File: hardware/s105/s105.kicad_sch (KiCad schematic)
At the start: 0 parts

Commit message: наименование цепей разъема
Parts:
- added P? (x2): 368255-2, hellen121vag:368255-2, symbol 368255-2:368255-2
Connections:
- net +5V: now also P?.32, P?.33
- new net +12V: P?.63
- new net +12_Sens: P?.44
- new net AC_Press: P?.21
- new net AC_Relay: P?.69
- new net AFR_1: P?.18
- new net AFR_1_Heater: P?.48
- new net AFR_2: P?.55
- new net Absorber: P?.46
- new net Atart_dis_Relay: P?.50
- new net CAM_in: P?.79
- new net CAN_H: P?.62
- new net CAN_L: P?.81
- new net CEL: P?.31
- new net CLT: P?.39
- new net Crank_Sens+: P?.15
- new net Crank_Sens-: P?.34
- new net DCNS: P?.75
- new net DIN1: P?.72
- new net DIN5: P?.76
- new net DPH2: P?.73
- new net ECO/CLT_Out: P?.10
- new net Fan_Relay_1: P?.68
- new net Fan_relay_2/Unk_Out_2: P?.30
- new net Fuel_Pump_Relay: P?.70
- new net GND: P?.3, P?.61, P?.80
- new net GNDA: P?.17, P?.20, P?.35, P?.36, P?.51, P?.52, P?.53, P?.54
- new net IAT: P?.40
- new net IGN_1: P?.5
- new net IGN_2: P?.2
- new net IGN_3: P?.4
- new net IGN_4: P?.1
- new net IGN_swt: P?.13
- new net INJ_1: P?.27
- new net INJ_2: P?.6
- new net INJ_3: P?.7
- new net INJ_4: P?.47
- new net INJ_6/AFR_2_Heater: P?.49
- new net INJ_7: P?.25
- new net Idle_valve_close: P?.28
- new net Idle_valve_open: P?.29
- new net K-line: P?.71
- new net Knock: P?.19
- new net MAF: P?.37
- new net MAP: P?.56
- new net Prog_mode: P?.43
- new net Speed_in: P?.59
- new net Start_req: P?.77
- new net TACH: P?.8
- new net TPS: P?.16
- new net Unk_Out_1: P?.9
- no-connect marks 0 -> 51
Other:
- added sheet MCU (stm32.kicad_sch)

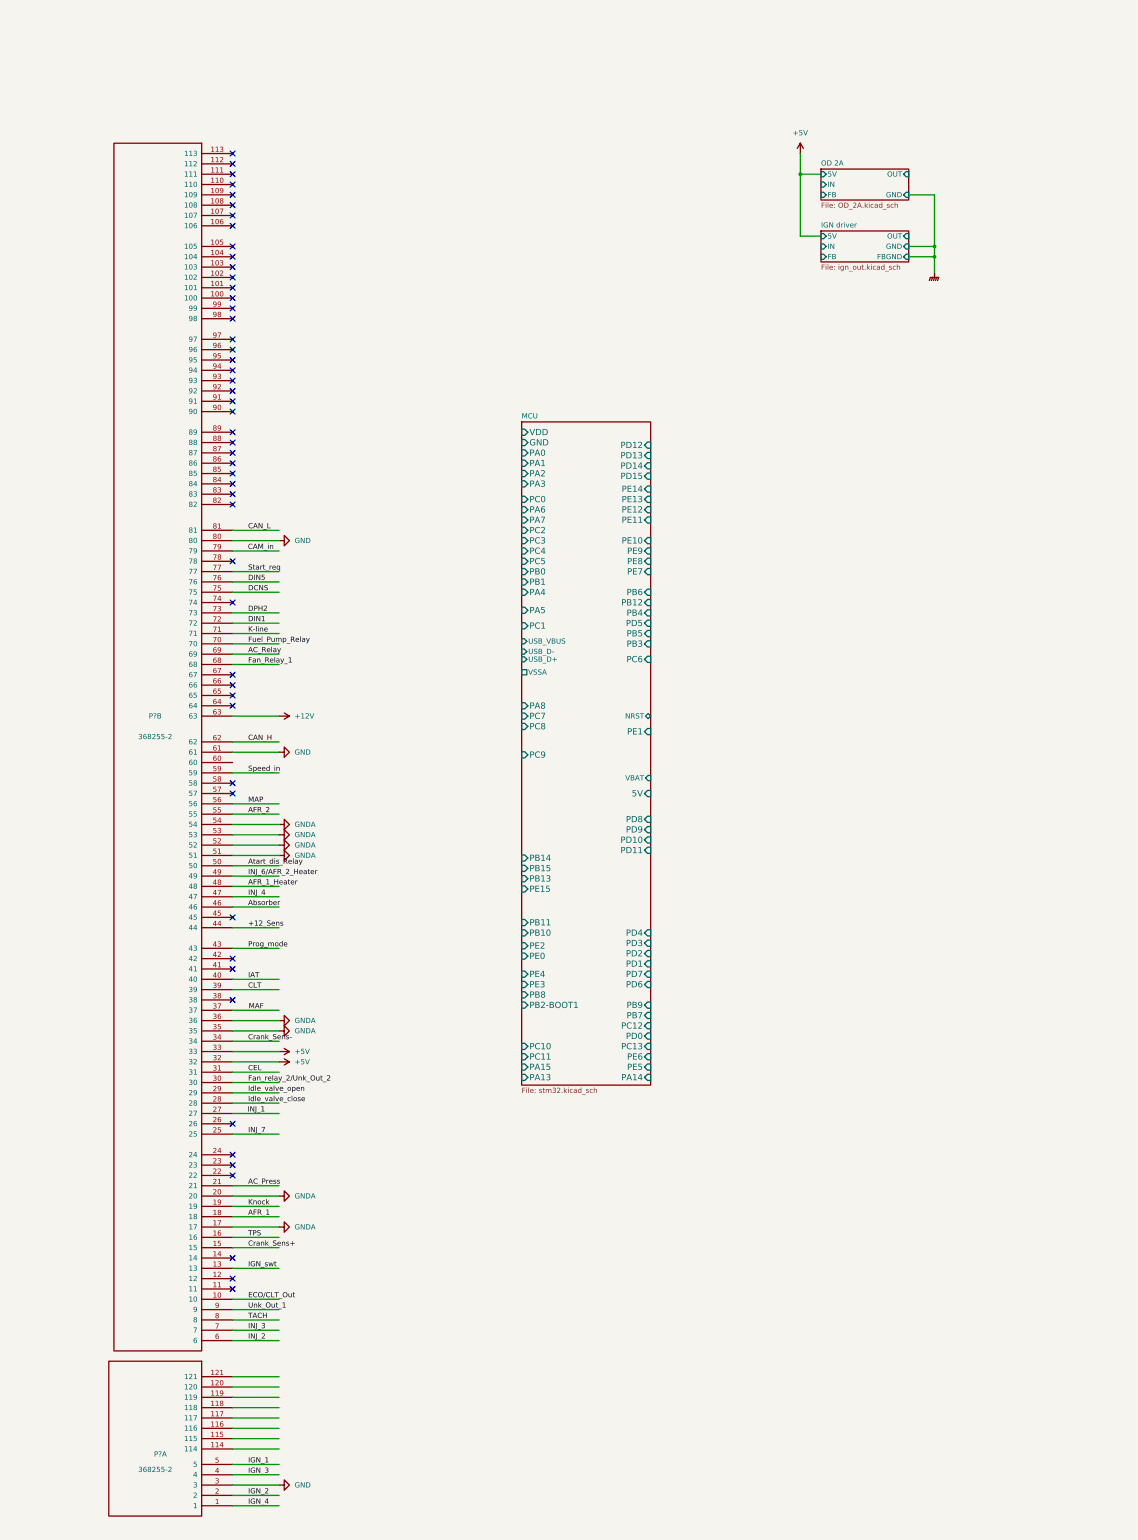
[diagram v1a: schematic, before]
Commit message: разместила схожие блоки
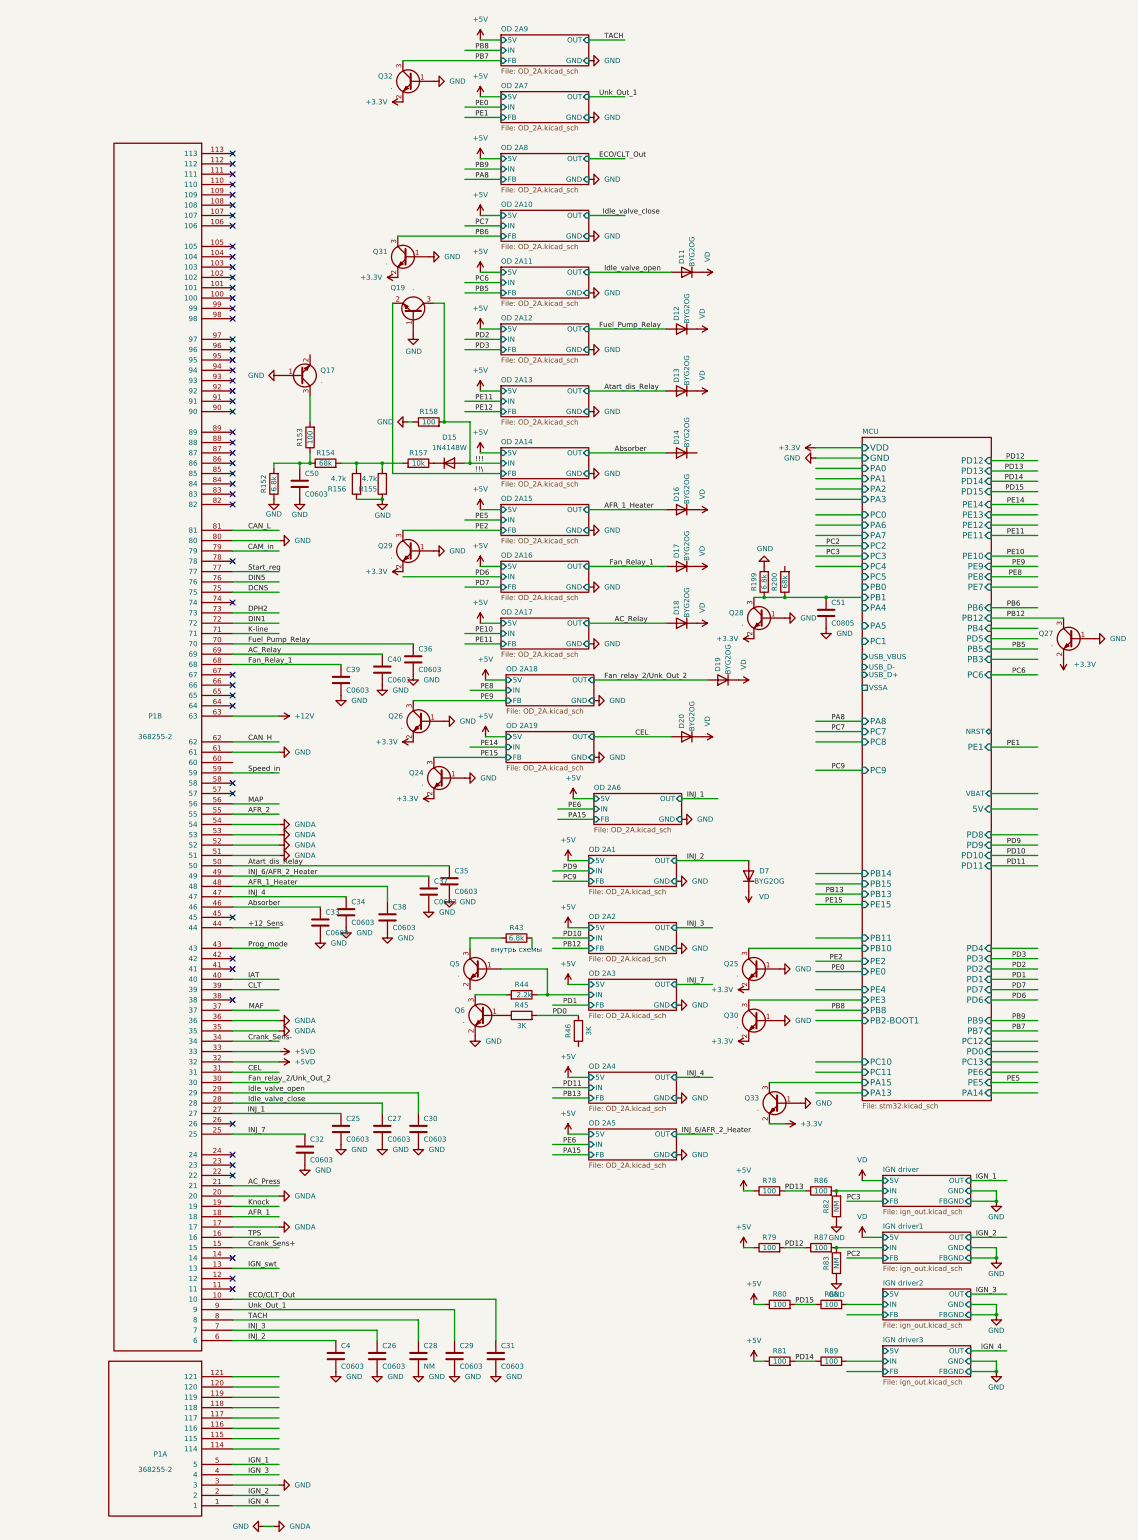
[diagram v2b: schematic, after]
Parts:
- added C25, C26, C27, C29, C30, C31, C32, C33, C34, C35, C36, C37, C38, C39, C4, C40, C50: C0603, Capacitor_SMD:C_0603_1608Metric, symbol Device:C
- added C28: NM, Capacitor_SMD:C_0603_1608Metric, symbol Device:C
- added C51: C0805, Capacitor_SMD:C_0805_2012Metric, symbol Device:C
- added D11, D12, D13, D14, D16, D17, D18, D19, D20, D7: BYG2OG, Diode_SMD:D_SMA, symbol Diode:US2JA
- added D15: 1N4148W, Diode_SMD:D_SOD-123, symbol Diode:1N4148W
- added Q17, Q19, Q24, Q25, Q26, Q27, Q28, Q29, Q30, Q31, Q32, Q33, Q5, Q6: ., Package_TO_SOT_SMD:SOT-23, symbol Transistor_BJT:BC847
- added R152, R199: 6.8k, Resistor_SMD:R_0603_1608Metric, symbol Device:R
- added R153, R158, R78, R79, R80, R81, R86, R87, R88, R89: 100, Resistor_SMD:R_0603_1608Metric, symbol Device:R
- added R154, R200: 68k, Resistor_SMD:R_0603_1608Metric, symbol Device:R
- added R155, R156: 4.7k, Resistor_SMD:R_1206_3216Metric, symbol Device:R
- added R157: 10k, Resistor_SMD:R_0805_2012Metric, symbol Device:R
- added R43: 6.8k, Resistor_SMD:R_0805_2012Metric, symbol Device:R
- added R44: 2.2k, Resistor_SMD:R_0805_2012Metric, symbol Device:R
- added R45, R46: 3K, Resistor_SMD:R_0603_1608Metric, symbol Device:R
- added R82, R83: NM, Resistor_SMD:R_0603_1608Metric, symbol Device:R
- gave numbers to parts that had none: 1
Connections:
- net GNDA is gone; now on net GND: P1.17, P1.20, P1.35, P1.36, P1.51, P1.52, P1.53, P1.54
- net +5V: now also R78.1, R79.1, R80.1, R81.1; no longer P1.32, P1.33
- net AC_Relay: now also C40.1, D18.2 (A)
- net AFR_1_Heater: now also C38.1, D16.2 (A)
- net Absorber: now also C33.1, D14.2 (A)
- net Atart_dis_Relay: now also C35.1, D13.2 (A)
- net CEL: now also D20.2 (A)
- net ECO/CLT_Out: now also C31.1
- net Fan_Relay_1: now also C39.1, D17.2 (A)
- net Fan_relay_2/Unk_Out_2: now also D19.2 (A)
- net Fuel_Pump_Relay: now also C36.1, D12.2 (A)
- net GND: now also C25.2, C26.2, C27.2, C28.2, C29.2, C30.2, C31.2, C32.2, C33.2, C34.2, C35.2, C36.2, C37.2, C38.2, C39.2, C4.2, C40.2, C50.2, C51.2, Q17.1 (B), Q19.1 (B), Q24.1 (B), Q25.1 (B), Q26.1 (B), Q27.1 (B), Q28.1 (B), Q29.1 (B), Q30.1 (B), Q31.1 (B), Q32.1 (B), Q33.1 (B), Q6.2 (E), R152.1, R155.1, R156.1, R158.1, R199.2, R82.1, R83.1
- net IGN driver/IN: now also R82.2, R86.2
- net INJ_1: now also C25.1
- net INJ_2: now also C4.1, D7.2 (A)
- net INJ_3: now also C26.1
- net INJ_4: now also C34.1
- net INJ_6/AFR_2_Heater: now also C37.1
- net INJ_7: now also C32.1
- net Idle_valve_close: now also C27.1
- net Idle_valve_open: now also C30.1, D11.2 (A)
- net MCU/PA15: now also Q33.3 (C)
- net MCU/PB1: now also C51.1, Q28.3 (C), R199.1, R200.1
- net MCU/PB10: now also Q25.3 (C)
- net MCU/PE3: now also Q30.3 (C)
- net TACH: now also C28.1
- net Unk_Out_1: now also C29.1
- new net: Q17.3 (C), R153.2
- new net: Q5.3 (C), R43.2
- new net: D15.1 (K), R157.1
- new net: R154.2, R155.2, R156.2, R157.2
- new net: C50.1, R152.2, R153.1, R154.1
- new net: Q6.1 (B), R45.1
- new net: Q6.3 (C), R44.2
- new net !!!: D15.2 (A), Q19.3 (C), R158.2
- new net !!\: Q19.2 (E)
- new net +3.3V: Q24.2 (E), Q25.2 (E), Q26.2 (E), Q27.2 (E), Q28.2 (E), Q29.2 (E), Q30.2 (E), Q31.2 (E), Q32.2 (E), Q33.2 (E)
- new net +5VD: P1.32, P1.33
- new net IGN driver1/IN: R83.2, R87.2
- new net IGN driver2/IN: R88.2
- new net IGN driver3/IN: R89.2
- new net OD 2A3/IN: Q5.1 (B), R44.1
- new net PB12: Q27.3 (C)
- new net PB6: Q31.3 (C)
- new net PB7: Q32.3 (C)
- new net PD0: R45.2, R46.2
- new net PD12: R79.2, R87.1
- new net PD13: R78.2, R86.1
- new net PD14: R81.2, R89.1
- new net PD15: R80.2, R88.1
- new net PE15: Q24.3 (C)
- new net PE2: Q29.3 (C)
- new net PE9: Q26.3 (C)
- new net VD: D11.1 (K), D12.1 (K), D13.1 (K), D16.1 (K), D17.1 (K), D18.1 (K), D19.1 (K), D20.1 (K), D7.1 (K)
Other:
- removed sheet OD 2A
- added sheet IGN driver1 (ign_out.kicad_sch)
- added sheet IGN driver2 (ign_out.kicad_sch)
- added sheet IGN driver3 (ign_out.kicad_sch)
- added sheet OD 2A1 (OD_2A.kicad_sch)
- added sheet OD 2A10 (OD_2A.kicad_sch)
- added sheet OD 2A11 (OD_2A.kicad_sch)
- added sheet OD 2A12 (OD_2A.kicad_sch)
- added sheet OD 2A13 (OD_2A.kicad_sch)
- added sheet OD 2A14 (OD_2A.kicad_sch)
- added sheet OD 2A15 (OD_2A.kicad_sch)
- added sheet OD 2A16 (OD_2A.kicad_sch)
- added sheet OD 2A17 (OD_2A.kicad_sch)
- added sheet OD 2A18 (OD_2A.kicad_sch)
- added sheet OD 2A19 (OD_2A.kicad_sch)
- added sheet OD 2A2 (OD_2A.kicad_sch)
- added sheet OD 2A3 (OD_2A.kicad_sch)
- added sheet OD 2A4 (OD_2A.kicad_sch)
- added sheet OD 2A5 (OD_2A.kicad_sch)
- added sheet OD 2A6 (OD_2A.kicad_sch)
- added sheet OD 2A7 (OD_2A.kicad_sch)
- added sheet OD 2A8 (OD_2A.kicad_sch)
- added sheet OD 2A9 (OD_2A.kicad_sch)
- note added: "внутрь схемы"

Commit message: вписала в габариты платы, продолжила опознание
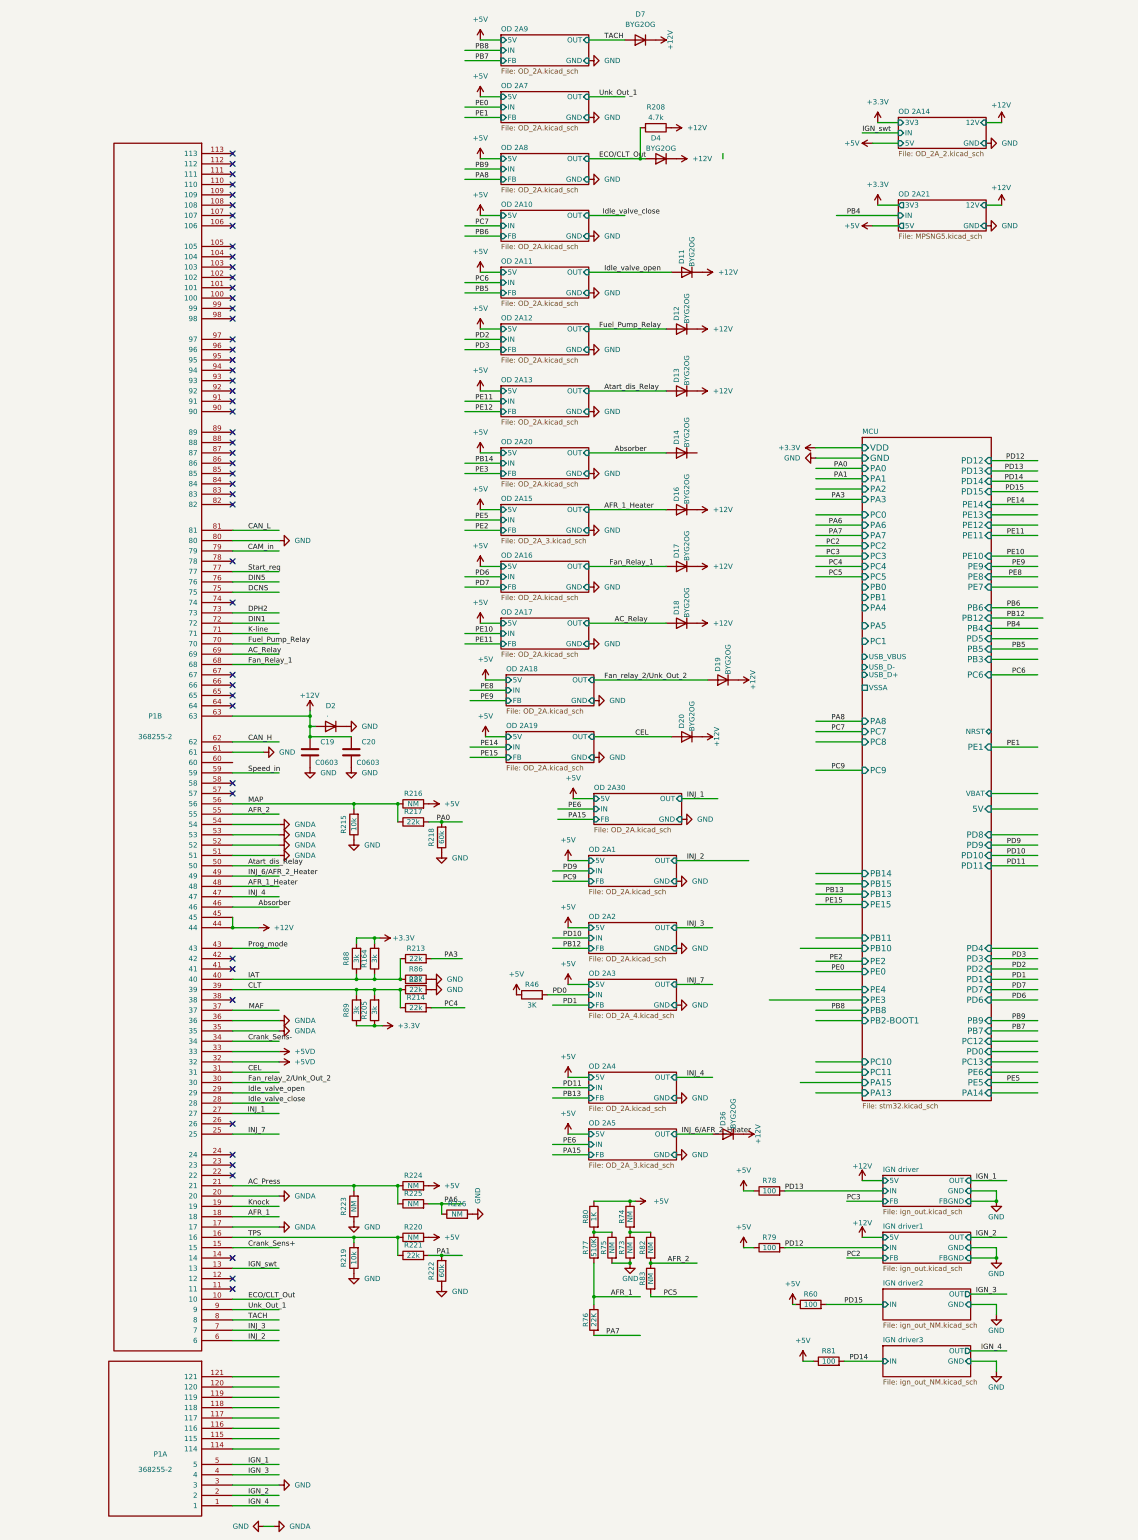
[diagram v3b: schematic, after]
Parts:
- removed C25, C26, C27, C29, C30, C31, C32, C33, C34, C35, C36, C37, C38, C39, C4, C40, C50: C0603, Capacitor_SMD:C_0603_1608Metric, symbol Device:C
- removed C28: NM, Capacitor_SMD:C_0603_1608Metric, symbol Device:C
- removed C51: C0805, Capacitor_SMD:C_0805_2012Metric, symbol Device:C
- removed D15: 1N4148W, Diode_SMD:D_SOD-123, symbol Diode:1N4148W
- removed Q17, Q19, Q24, Q25, Q26, Q27, Q28, Q29, Q30, Q31, Q32, Q33, Q5, Q6: ., Package_TO_SOT_SMD:SOT-23, symbol Transistor_BJT:BC847
- removed R152, R199: 6.8k, Resistor_SMD:R_0603_1608Metric, symbol Device:R
- removed R153, R158: 100, Resistor_SMD:R_0603_1608Metric, symbol Device:R
- removed R154, R200: 68k, Resistor_SMD:R_0603_1608Metric, symbol Device:R
- removed R155, R156: 4.7k, Resistor_SMD:R_1206_3216Metric, symbol Device:R
- removed R157: 10k, Resistor_SMD:R_0805_2012Metric, symbol Device:R
- removed R43: 6.8k, Resistor_SMD:R_0805_2012Metric, symbol Device:R
- removed R44: 2.2k, Resistor_SMD:R_0805_2012Metric, symbol Device:R
- removed R45: 3K, Resistor_SMD:R_0603_1608Metric, symbol Device:R
- added C19, C20: C0603, Capacitor_SMD:C_0603_1608Metric, symbol Device:C
- added D2: ., Diode_SMD:D_SMC, symbol Diode:US2JA
- added D36, D4: BYG2OG, Diode_SMD:D_SMA, symbol Diode:US2JA
- added R164, R205: 3k, Resistor_SMD:R_1206_3216Metric, symbol Device:R
- added R208: 4.7k, Resistor_SMD:R_1206_3216Metric, symbol Device:R
- added R213, R214, R217, R221: 22k, Resistor_SMD:R_0603_1608Metric, symbol Device:R
- added R215, R219: 10k, Resistor_SMD:R_0603_1608Metric, symbol Device:R
- added R216, R220, R223, R224, R225, R226, R73, R74, R75: NM, Resistor_SMD:R_0603_1608Metric, symbol Device:R
- added R218, R222: 60k, Resistor_SMD:R_0603_1608Metric, symbol Device:R
- added R60: 100, Resistor_SMD:R_0603_1608Metric, symbol Device:R
- added R76: 22K, Resistor_SMD:R_0603_1608Metric, symbol Device:R
- added R77: 510K, Resistor_SMD:R_0603_1608Metric, symbol Device:R
- R80: value 100 -> 1K; LCSC (none) -> C25804; Manufacturer (none) -> StackPole; Part # (none) -> RMCF0603JT10K0; VEND (none) -> DIGI; VEND# (none) -> RMCF0603JT10K0CT-ND
- R82, R83: LCSC (none) -> C25804; Manufacturer (none) -> StackPole; Part # (none) -> RMCF0603JT10K0; VEND (none) -> DIGI; VEND# (none) -> RMCF0603JT10K0CT-ND
- R86, R87: value 100 -> 22k
- R88, R89: value 100 -> 3k; footprint Resistor_SMD:R_0603_1608Metric -> Resistor_SMD:R_1206_3216Metric
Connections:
- net +12_Sens is gone; now on net +12V: P1.44
- net IGN driver2/IN is gone; now on net +3.3V: R88.2
- net IGN driver3/IN is gone; now on net CLT: R89.2
- net VD is gone; now on net +12V: D11.1 (K), D12.1 (K), D13.1 (K), D16.1 (K), D17.1 (K), D18.1 (K), D19.1 (K), D20.1 (K), D7.1 (K)
- net +12V: now also P1.45, C19.1, C20.1, D2.2 (A), D36.1 (K), D4.1 (K), R208.1
- net +3.3V: now also R89.1, R164.2, R205.1
- net +5V: now also R46.1, R216.2, R220.2, R224.2, R60.1, R74.1
- net AC_Press: now also R223.2, R224.1, R225.1
- net AFR_1: now also R76.1, R77.2
- net AFR_2: now also R82.2, R83.1
- net CLT: now also R87.1, R205.2, R214.1
- net ECO/CLT_Out: now also D4.2 (A), R208.2
- net GND: now also R86.2, R87.2, C19.2, C20.2, D2.1 (K), R215.1, R218.1, R219.1, R222.1, R223.1, R226.2, R73.2, R75.2; no longer R82.1, R83.1
- net IAT: now also R86.1, R88.1, R164.1, R213.1
- net INJ_2: no longer D7.2 (A)
- net INJ_6/AFR_2_Heater: now also D36.2 (A)
- net MAP: now also R215.2, R216.1, R217.1
- net PD12: no longer R87.1
- net PD13: no longer R86.1
- net PD14: no longer R89.1
- net PD15: now also R60.2; no longer R80.2, R88.1
- net TACH: now also D7.2 (A)
- net TPS: now also R219.2, R220.1, R221.1
- removed net IGN driver/IN: R82.2, R86.2
- net IGN driver1/IN renamed PC5
- net PC5: no longer R87.2
- new net: R73.1, R74.2, R82.1
- new net: R75.1, R77.1, R80.2
- new net PA0: R217.2, R218.2
- new net PA1: R221.2, R222.2
- new net PA3: R213.2
- new net PA6: R225.2, R226.1
- new net PA7: R76.2
- new net PC4: R214.2
- no-connect marks 51 -> 50
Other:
- sheet OD 2A6 renamed OD 2A30
- added sheet OD 2A20 (OD_2A.kicad_sch)
- added sheet OD 2A21 (MPSNG5.kicad_sch)
- sheet IGN driver2: file ign_out.kicad_sch -> ign_out_NM.kicad_sch
- sheet IGN driver2 ports: added none; removed 5V, FB, FBGND
- sheet IGN driver3: file ign_out.kicad_sch -> ign_out_NM.kicad_sch
- sheet IGN driver3 ports: added none; removed 5V, FB, FBGND
- sheet OD 2A14: file OD_2A.kicad_sch -> OD_2A_2.kicad_sch
- sheet OD 2A14 ports: added 12V, 3V3; removed FB, OUT
- sheet OD 2A15: file OD_2A.kicad_sch -> OD_2A_3.kicad_sch
- sheet OD 2A3: file OD_2A.kicad_sch -> OD_2A_4.kicad_sch
- sheet OD 2A5: file OD_2A.kicad_sch -> OD_2A_3.kicad_sch
- note removed: "внутрь схемы"
- moved on the sheet: D7, R46, R81
